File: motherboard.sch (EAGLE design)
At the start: 159 parts, among them IC1 LM2576, IC10 TUSB2046B, IC11 OPA129U, IC12 LM50, IC13 LM50, IC2 74LS595D, IC3 74LS595D, IC4 IC_FT230X-SSOP-16, IC5 VN5772AK, IC6 VN5772AK, IC7 VN5772AK, IC8 VN5772AK, IC9 VN5772AK, U2 NCP4625, U3 ATMEGA168, Y1 16Mhz, Y2 6MHz

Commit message: finished subsystem validatation
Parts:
- removed C43, C44, C45: (no value), adafruit:C-USC1206
- removed F4: 500mA, dp_devices:FUSE_PTC-1812
- removed IC11: OPA129U, burr-brown:OPA129U
- removed JP11: (no value), sparkfun:M023.5MM
- removed JP12, JP13: (no value), SparkFun-Connectors:M063.5MM-6
- removed LED1, LED2: (no value), adafruit:LEDCHIPLED_1206
- added C23: 0.1uF, adafruit:C-USC1206
- added D12, D13, D14, D15, D16, D17, D18, D19, D20, D21: (no value), adafruit:DIODESMA
- added F5, F6, F7, F8: (no value), special:FUSE2P
- added ISP2, ISP3, ISP4, ISP5: AVRISP-6, adafruit:AVRISP-6
- added R38, R39: 10k, adafruit:R-US_R1206
- added U$10, U$11, U$12, U$13, U$14, U$15, U$16, U$6, U$7, U$8, U$9: TVS, sparkfun:TVS
- added ZD1, ZD3, ZD4, ZD5: 5V, dp_devices:ZENERSOD-123
- C10, C4: value 1000uF -> 500uF
- C13: value 1000uF -> 4.7uF; device adafruit:CPOL-US153CLV-0807 -> adafruit:C-USC1206
- C14: value 0.1uF -> 500uF; device adafruit:C-USC1206 -> adafruit:CPOL-US153CLV-0807
- C15: value 1uF -> 0.1uF
- C16: value 1000uF -> 1uF; device adafruit:CPOL-US153CLV-0807 -> adafruit:C-USC1206
- C17: value 0.1uF -> 4.7uF
- C18: value 1uF -> 500uF; device adafruit:C-USC1206 -> adafruit:CPOL-US153CLV-0807
- C19: value 1000uF -> 0.1uF; device adafruit:CPOL-US153CLV-0807 -> adafruit:C-USC1206
- C20: value 0.1uF -> 1uF
- C21: value 1uF -> 4.7uF
- C24, C25, C26, C27, C28, C29, C30, C32, C33, C9: value (none) -> 47pF
- C35: value (none) -> 4.7uF
- C36: value (none) -> 0.1uF
- C39: value 4.7uF -> 500uF; device adafruit:C-USC1206 -> adafruit:CPOL-US153CLV-0807
- C40: value 4.7uF -> 0.1uF
- C41: value 4.7uF -> 1uF
- D10, D11, D2, D3, D4, D5, D6, D7, D8, D9: value BAV199 -> (none); device diode:BAV199 -> adafruit:DIODESMA
- R10, R36, R37, R6, R7, R8, R9: value 10k -> 1k
- R12, R13, R16, R17, R18, R19, R20, R21, R28, R29: value (none) -> 27
- R14, R15, R22, R23, R24, R25, R27, R30: value (none) -> 15k
- R26, R31, R5: value (none) -> 1k
- R32, R33: value (none) -> 10k
- ZD2: value (none) -> 5V
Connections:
- removed net !USB_RST: R26.2, U3.PD7(AIN1)
- removed net ARM_EN: R37.2, U3.PB1(OC1A)
- removed net CONDUCT: IC11.-IN, IC11.OUT, U3.ADC7
- removed net N$16: C18.2, D8.AC, IC8.DRAIN4@0, IC8.DRAIN4@1, IC8.DRAIN4@2, IC8.DRAIN4@3, IC8.SOURCE2@0, IC8.SOURCE2@1, JP5.2
- removed net N$17: C21.1, D11.AC, IC9.DRAIN3@0, IC9.DRAIN3@1, IC9.DRAIN3@2, IC9.DRAIN3@3, IC9.SOURCE1@0, IC9.SOURCE1@1, JP6.1
- removed net N$18: C21.2, D10.AC, IC9.DRAIN4@0, IC9.DRAIN4@1, IC9.DRAIN4@2, IC9.DRAIN4@3, IC9.SOURCE2@0, IC9.SOURCE2@1, JP6.2
- removed net N$56: JP13.5, R37.1
- removed net RANG_EN: R36.2, U3.PB0(ICP)
- new net EN1: R39.2, U3.ADC7
- new net EN2: R38.2, U3.PD7(AIN1)
- new net EN3: R33.2, U3.PB0(ICP)
- new net EN4: R32.2, U3.PB1(OC1A)
- new net N$20: C56.+, F8.1A, JP17.1, U$9.2
- new net N$54: C54.+, F6.1A, JP15.1, U$7.2
- new net N$58: ISP5.RST, R39.1, U$14.2
- net +12V: now also C13.1, C14.+, C15.1, C18.+, C19.1, C21.1, C39.+, D12.C, D14.C, D16.C, D18.C, D20.C, F5.2A, F6.2A, F7.2A, F8.2A; no longer C13.+, C14.1, C16.+, C19.+, C20.1, C39.1, C41.1, C53.+, C54.+, C55.+, C56.+, D11.C, D3.C, D5.C, D7.C, D9.C, JP14.1, JP15.1, JP16.1, JP17.1
- net +5V: now also ISP2.VCC, ISP3.VCC, ISP4.VCC, ISP5.VCC, U$16.2; no longer C43.1, C44.1, F4.2, IC11.V+, JP12.1, JP13.1
- net 0SENSE: now also IC6.SENSE, IC7.SENSE, IC8.SENSE, IC9.SENSE, R26.1, R36.1, R5.1, R6.2, R7.1, R9.1, ZD1.C
- net 1SENSE: now also R7.2, R8.1, ZD2.C; no longer IC6.SENSE, R7.1
- net 2SENSE: now also R10.1, R9.2, ZD3.C; no longer IC7.SENSE, R8.1
- net 3.3V: now also IC10.!RST
- net 3SENSE: now also R26.2, R31.1, ZD4.C; no longer IC8.SENSE, R9.1
- net 4SENSE: now also R36.2, R37.1, ZD5.C; no longer IC9.SENSE, R10.1
- net AGND: no longer C43.2, C44.2, C45.2, IC11.V-, JP11.2, R33.2, U$5.1
- net GND: now also C13.2, C14.-, C15.2, C18.-, C19.2, C21.2, C23.2, C39.-, D13.A, D15.A, D17.A, D19.A, D21.A, ISP2.GND, ISP3.GND, ISP4.GND, ISP5.GND, R31.2, R37.2, R5.2, U$10.1, U$11.1, U$12.1, U$13.1, U$14.1, U$15.1, U$16.1, U$5.1, U$6.1, U$7.1, U$8.1, U$9.1, ZD1.A, ZD3.A, ZD4.A, ZD5.A; no longer C13.-, C14.2, C16.-, C19.-, C20.2, C39.2, C41.2, D10.A, D2.A, D4.A, D6.A, D8.A, JP12.6, JP13.6, R6.2, R7.2, R9.2
- net MISO: now also ISP2.MISO, ISP3.MISO, ISP4.MISO, ISP5.MISO, U$10.2; no longer JP12.3, JP13.3
- net MOSI: now also ISP2.MOSI, ISP3.MOSI, ISP4.MOSI, ISP5.MOSI, U$11.2; no longer JP12.2, JP13.2
- net N$10: now also C20.1, D10.A, D11.C, IC8.DRAIN3@0, IC8.DRAIN3@1, IC8.DRAIN3@2, IC8.DRAIN3@3, IC8.SOURCE1@0, IC8.SOURCE1@1, JP5.1; no longer C12.2, D4.AC, IC6.DRAIN4@0, IC6.DRAIN4@1, IC6.DRAIN4@2, IC6.DRAIN4@3, IC6.SOURCE2@0, IC6.SOURCE2@1, JP3.2
- net N$11: now also D2.A, D3.C; no longer D3.AC
- net N$12: now also C20.2, D12.A, D13.C, IC8.DRAIN4@0, IC8.DRAIN4@1, IC8.DRAIN4@2, IC8.DRAIN4@3, IC8.SOURCE2@0, IC8.SOURCE2@1, JP5.2; no longer C15.1, D7.AC, IC7.DRAIN3@0, IC7.DRAIN3@1, IC7.DRAIN3@2, IC7.DRAIN3@3, IC7.SOURCE1@0, IC7.SOURCE1@1, JP4.1
- net N$13: now also D4.A, D5.C; no longer D2.AC
- net N$14: now also C41.1, D6.A, D7.C, IC9.DRAIN3@0, IC9.DRAIN3@1, IC9.DRAIN3@2, IC9.DRAIN3@3, IC9.SOURCE1@0, IC9.SOURCE1@1, JP6.1; no longer C15.2, D6.AC, IC7.DRAIN4@0, IC7.DRAIN4@1, IC7.DRAIN4@2, IC7.DRAIN4@3, IC7.SOURCE2@0, IC7.SOURCE2@1, JP4.2
- net N$15: now also C41.2, D8.A, D9.C, IC9.DRAIN4@0, IC9.DRAIN4@1, IC9.DRAIN4@2, IC9.DRAIN4@3, IC9.SOURCE2@0, IC9.SOURCE2@1, JP6.2; no longer C18.1, D9.AC, IC8.DRAIN3@0, IC8.DRAIN3@1, IC8.DRAIN3@2, IC8.DRAIN3@3, IC8.SOURCE1@0, IC8.SOURCE1@1, JP5.1
- net N$3: now also D18.A, D19.C; no longer D5.AC
- net N$38: now also C23.1; no longer R31.1, R32.1
- net N$5: now also C12.2, D20.A, D21.C, IC6.DRAIN4@0, IC6.DRAIN4@1, IC6.DRAIN4@2, IC6.DRAIN4@3, IC6.SOURCE2@0, IC6.SOURCE2@1, JP3.2; no longer IC10.!RST, R26.1, ZD2.C
- net N$50: now also C55.+, F7.1A, JP16.1, U$8.2; no longer IC4.CBUS1, LED1.C
- net N$51: now also ISP2.RST, R32.1, U$13.2; no longer IC4.CBUS2, LED2.C
- net N$52: now also ISP3.RST, R33.1, U$15.2; no longer LED1.A, R31.2
- net N$53: now also ISP4.RST, R38.1, U$12.2; no longer LED2.A, R32.2
- net N$55: now also C53.+, F5.1A, JP14.1, U$6.2; no longer JP12.5, R36.1
- net N$8: now also C16.1, D14.A, D15.C, IC7.DRAIN3@0, IC7.DRAIN3@1, IC7.DRAIN3@2, IC7.DRAIN3@3, IC7.SOURCE1@0, IC7.SOURCE1@1, JP4.1; no longer F4.1, R5.1
- net N$9: now also C16.2, D16.A, D17.C, IC7.DRAIN4@0, IC7.DRAIN4@1, IC7.DRAIN4@2, IC7.DRAIN4@3, IC7.SOURCE2@0, IC7.SOURCE2@1, JP4.2; no longer C45.1, IC11.+IN, JP11.1, R33.1, R5.2, U$5.2
- net SCK: now also ISP2.SCK, ISP3.SCK, ISP4.SCK, ISP5.SCK, U$5.2; no longer JP12.4, JP13.4
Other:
- moved on the sheet: C1, C10, C11, C12, C15, C17, C2, C20, C21, C22, C24, C25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

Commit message: updated sch
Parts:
- added SW1: FSMSM, alcoswitch:FSMSM
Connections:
- net EN1 renamed !EN1
- net EN2 renamed !EN2
- net EN3 renamed !EN3
- net EN4 renamed !EN4
- net !RST: now also SW1.S
- net GND: now also SW1.P
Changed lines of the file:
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@@
 <grid distance="0.1" unitdist="inch" unit="inch" style="lines" multiple="1" display="no" altdistance="0.01" altunitdist="inch" altunit="inch"/>
 <layers>
-<layer number="1" name="Top" color="4" fill="1" visible="yes" active="no"/>
-<layer number="2" name="Route2" color="1" fill="3" visible="yes" active="no"/>
-<layer number="3" name="Route3" color="4" fill="3" visible="yes" active="no"/>
-<layer number="4" name="Route4" color="1" fill="4" visible="yes" active="no"/>
-<layer number="5" name="Route5" color="4" fill="4" visible="yes" active="no"/>
-<layer number="6" name="Route6" color="1" fill="8" visible="yes" active="no"/>
-<layer number="7" name="Route7" color="4" fill="8" visible="yes" active="no"/>
-<layer number="8" name="Route8" color="1" fill="2" visible="yes" active="no"/>
-<layer number="9" name="Route9" color="4" fill="2" visible="yes" active="no"/>
-<layer number="10" name="Route10" color="1" fill="7" visible="yes" active="no"/>
-<layer number="11" name="Route11" color="4" fill="7" visible="yes" active="no"/>
-<layer number="12" name="Route12" color="1" fill="5" visible="yes" active="no"/>
-<layer number="13" name="Route13" color="4" fill="5" visible="yes" active="no"/>
-<layer number="14" name="Route14" color="1" fill="6" visible="yes" active="no"/>
-<layer number="15" name="Route15" color="4" fill="6" visible="yes" active="no"/>
-<layer number="16" name="Bottom" color="1" fill="1" visible="yes" active="no"/>
-<layer number="17" name="Pads" color="2" fill="1" visible="yes" active="no"/>
-<layer number="18" name="Vias" color="2" fill="1" visible="yes" active="no"/>
-<layer number="19" name="Unrouted" color="6" fill="1" visible="yes" active="no"/>
-<layer number="20" name="Dimension" color="15" fill="1" visible="yes" active="no"/>
-<layer number="21" name="tPlace" color="7" fill="1" visible="yes" active="no"/>
-<layer number="22" name="bPlace" color="7" fill="1" visible="yes" active="no"/>
-<layer number="23" name="tOrigins" color="15" fill="1" visible="yes" active="no"/>
-<layer number="24" name="bOrigins" color="15" fill="1" visible="yes" active="no"/>
-<layer number="25" name="tNames" color="7" fill="1" visible="yes" active="no"/>
-<layer number="26" name="bNames" color="7" fill="1" visible="yes" active="no"/>
-<layer number="27" name="tValues" color="7" fill="1" visible="yes" active="no"/>
-<layer number="28" name="bValues" color="7" fill="1" visible="yes" active="no"/>
+<layer number="1" name="Top" color="4" fill="1" visible="no" active="no"/>
+<layer number="2" name="Route2" color="1" fill="3" visible="no" active="no"/>
+<layer number="3" name="Route3" color="4" fill="3" visible="no" active="no"/>
+<layer number="4" name="Route4" color="1" fill="4" visible="no" active="no"/>
+<layer number="5" name="Route5" color="4" fill="4" visible="no" active="no"/>
+<layer number="6" name="Route6" color="1" fill="8" visible="no" active="no"/>
+<layer number="7" name="Route7" color="4" fill="8" visible="no" active="no"/>
+<layer number="8" name="Route8" color="1" fill="2" visible="no" active="no"/>
+<layer number="9" name="Route9" color="4" fill="2" visible="no" active="no"/>
+<layer number="10" name="Route10" color="1" fill="7" visible="no" active="no"/>
+<layer number="11" name="Route11" color="4" fill="7" visible="no" active="no"/>
+<layer number="12" name="Route12" color="1" fill="5" visible="no" active="no"/>
+<layer number="13" name="Route13" color="4" fill="5" visible="no" active="no"/>
+<layer number="14" name="Route14" color="1" fill="6" visible="no" active="no"/>
+<layer number="15" name="Route15" color="4" fill="6" visible="no" active="no"/>
+<layer number="16" name="Bottom" color="1" fill="1" visible="no" active="no"/>
+<layer number="17" name="Pads" color="2" fill="1" visible="no" active="no"/>
+<layer number="18" name="Vias" color="2" fill="1" visible="no" active="no"/>
+<layer number="19" name="Unrouted" color="6" fill="1" visible="no" active="no"/>
+<layer number="20" name="Dimension" color="15" fill="1" visible="no" active="no"/>
+<layer number="21" name="tPlace" color="7" fill="1" visible="no" active="no"/>
+<layer number="22" name="bPlace" color="7" fill="1" visible="no" active="no"/>
+<layer number="23" name="tOrigins" color="15" fill="1" visible="no" active="no"/>
+<layer number="24" name="bOrigins" color="15" fill="1" visible="no" active="no"/>
+<layer number="25" name="tNames" color="7" fill="1" visible="no" active="no"/>
+<layer number="26" name="bNames" color="7" fill="1" visible="no" active="no"/>
+<layer number="27" name="tValues" color="7" fill="1" visible="no" active="no"/>
+<layer number="28" name="bValues" color="7" fill="1" visible="no" active="no"/>
 <layer number="29" name="tStop" color="7" fill="3" visible="no" active="no"/>
 <layer number="30" name="bStop" color="7" fill="6" visible="no" active="no"/>
@@
 <layer number="35" name="tGlue" color="7" fill="4" visible="no" active="no"/>
 <layer number="36" name="bGlue" color="7" fill="5" visible="no" active="no"/>
-<layer number="37" name="tTest" color="7" fill="1" visible="yes" active="no"/>
-<layer number="38" name="bTest" color="7" fill="1" visible="yes" active="no"/>
+<layer number="37" name="tTest" color="7" fill="1" visible="no" active="no"/>
+<layer number="38" name="bTest" color="7" fill="1" visible="no" active="no"/>
 <layer number="39" name="tKeepout" color="4" fill="11" visible="no" active="no"/>
 <layer number="40" name="bKeepout" color="1" fill="11" visible="no" active="no"/>
@@
 <layer number="44" name="Drills" color="7" fill="1" visible="no" active="no"/>
 <layer number="45" name="Holes" color="7" fill="1" visible="no" active="no"/>
-<layer number="46" name="Milling" color="3" fill="1" visible="yes" active="no"/>
-<layer number="47" name="Measures" color="7" fill="1" visible="yes" active="no"/>
-<layer number="48" name="Document" color="7" fill="1" visible="yes" active="no"/>
-<layer number="49" name="Reference" color="7" fill="1" visible="yes" active="no"/>
-<layer number="50" name="dxf" color="7" fill="1" visible="yes" active="no"/>
-<layer number="51" name="tDocu" color="6" fill="1" visible="yes" active="no"/>
-<layer number="52" name="bDocu" color="7" fill="1" visible="yes" active="no"/>
-<layer number="53" name="tGND_GNDA" color="7" fill="9" visible="yes" active="no"/>
-<layer number="54" name="bGND_GNDA" color="1" fill="9" visible="yes" active="no"/>
-<layer number="56" name="wert" color="7" fill="1" visible="yes" active="no"/>
-<layer number="57" name="tCAD" color="7" fill="1" visible="yes" active="no"/>
+<layer number="46" name="Milling" color="3" fill="1" visible="no" active="no"/>
+<layer number="47" name="Measures" color="7" fill="1" visible="no" active="no"/>
+<layer number="48" name="Document" color="7" fill="1" visible="no" active="no"/>
+<layer number="49" name="Reference" color="7" fill="1" visible="no" active="no"/>
+<layer number="50" name="dxf" color="7" fill="1" visible="no" active="no"/>
+<layer number="51" name="tDocu" color="6" fill="1" visible="no" active="no"/>
+<layer number="52" name="bDocu" color="7" fill="1" visible="no" active="no"/>
+<layer number="53" name="tGND_GNDA" color="7" fill="9" visible="no" active="no"/>
+<layer number="54" name="bGND_GNDA" color="1" fill="9" visible="no" active="no"/>
+<layer number="56" name="wert" color="7" fill="1" visible="no" active="no"/>
+<layer number="57" name="tCAD" color="7" fill="1" visible="no" active="no"/>
 <layer number="91" name="Nets" color="2" fill="1" visible="yes" active="yes"/>
 <layer number="92" name="Busses" color="1" fill="1" visible="yes" active="yes"/>
@@
 <part name="D20" library="adafruit" deviceset="DIODE" device="SMA"/>
 <part name="D21" library="adafruit" deviceset="DIODE" device="SMA"/>
+<part name="SW1" library="alcoswitch" deviceset="FSMSM" device="" value=""/>
+<part name="GND117" library="sparkfun" deviceset="GND" device=""/>
 </parts>
 <sheets>
@@
 <instance part="D20" gate="G$1" x="365.76" y="127" rot="R90"/>
 <instance part="D21" gate="G$1" x="365.76" y="116.84" rot="R90"/>
+<instance part="SW1" gate="G$1" x="86.36" y="226.06"/>
+<instance part="GND117" gate="1" x="86.36" y="215.9"/>
 </instances>
 <busses>
@@
 <pinref part="GND116" gate="1" pin="GND"/>
 </segment>
+<segment>
+<pinref part="SW1" gate="G$1" pin="P"/>
+<pinref part="GND117" gate="1" pin="GND"/>
+<wire x1="86.36" y1="218.44" x2="86.36" y2="220.98" width="0.1524" layer="91"/>
+</segment>
 </net>
 <net name="+5V" class="0">
@@
 <label x="78.74" y="233.68" size="1.778" layer="95"/>
 <pinref part="U3" gate="G$1" pin="PC6(/RESET)"/>
+<pinref part="SW1" gate="G$1" pin="S"/>
+<wire x1="86.36" y1="231.14" x2="86.36" y2="233.68" width="0.1524" layer="91"/>
 </segment>
 <segment>
@@
 </segment>
 </net>
-<net name="EN4" class="0">
+<net name="!EN4" class="0">
 <segment>
 <pinref part="U3" gate="G$1" pin="PB1(OC1A)"/>
@@
 </segment>
 </net>
-<net name="EN3" class="0">
+<net name="!EN3" class="0">
 <segment>
 <pinref part="U3" gate="G$1" pin="PB0(ICP)"/>
@@
 </segment>
 </net>
-<net name="EN1" class="0">
+<net name="!EN1" class="0">
 <segment>
 <pinref part="U3" gate="G$1" pin="ADC7"/>
@@
 </segment>
 </net>
-<net name="EN2" class="0">
+<net name="!EN2" class="0">
 <segment>
 <pinref part="U3" gate="G$1" pin="PD7(AIN1)"/>

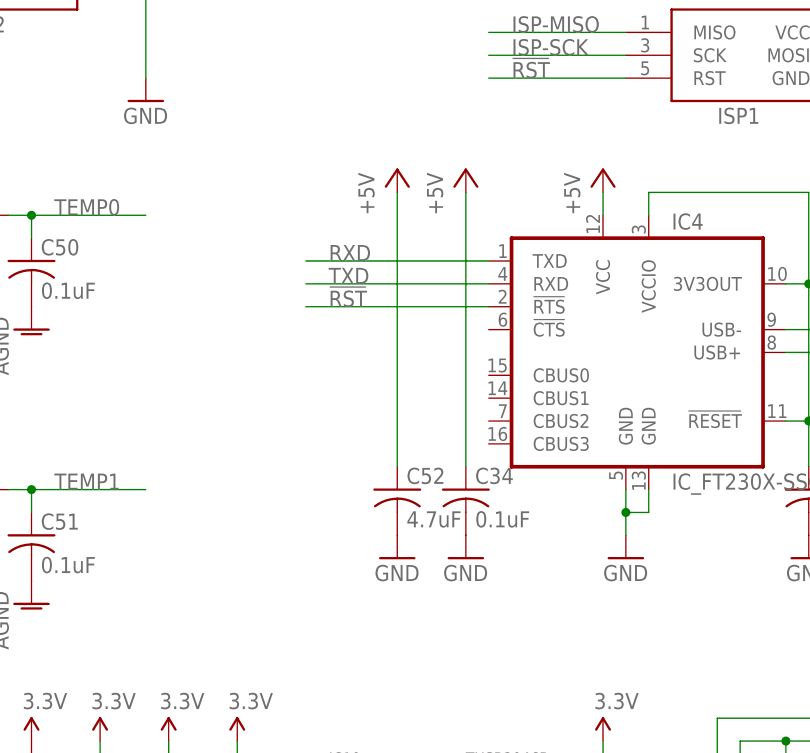
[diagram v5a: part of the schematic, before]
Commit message: added missing reset capacitor
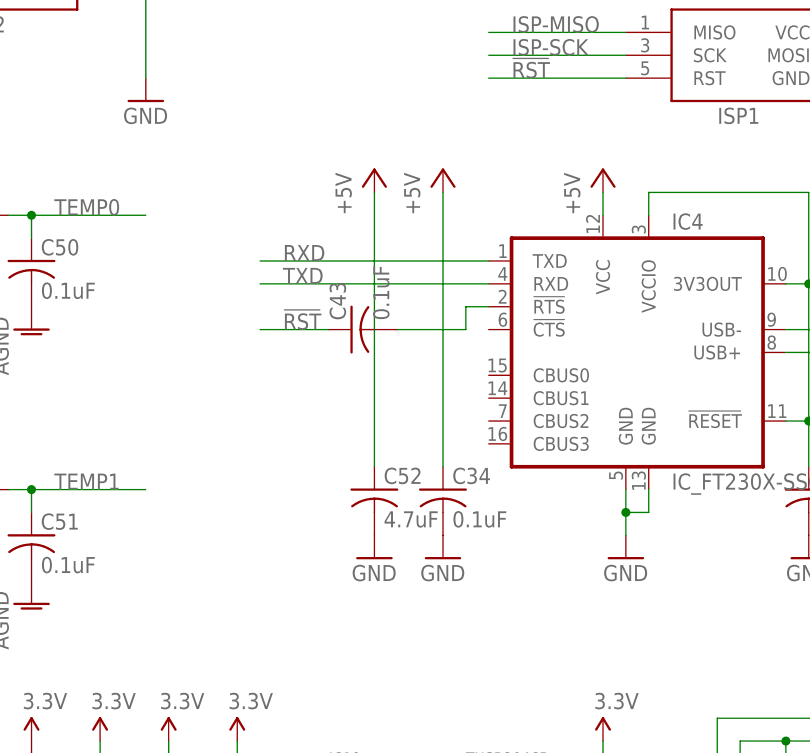
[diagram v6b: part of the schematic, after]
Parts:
- added C43: 0.1uF, adafruit:C-USC1206
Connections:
- new net N$16: C43.2, IC4.!RTS
- net !RST: now also C43.1; no longer IC4.!RTS
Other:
- moved on the sheet: C34, C52
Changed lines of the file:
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@@
 <part name="SW1" library="alcoswitch" deviceset="FSMSM" device="" value=""/>
 <part name="GND117" library="sparkfun" deviceset="GND" device=""/>
+<part name="C43" library="adafruit" deviceset="C-US" device="C1206" value="0.1uF"/>
 </parts>
 <sheets>
@@
 <instance part="GND76" gate="1" x="154.94" y="91.44"/>
 <instance part="GND77" gate="1" x="162.56" y="91.44"/>
-<instance part="C34" gate="G$1" x="88.9" y="99.06"/>
+<instance part="C34" gate="G$1" x="86.36" y="99.06"/>
 <instance part="C35" gate="G$1" x="48.26" y="45.72"/>
 <instance part="C36" gate="G$1" x="55.88" y="45.72"/>
@@
 <instance part="GND78" gate="1" x="48.26" y="2.54"/>
 <instance part="GND79" gate="1" x="55.88" y="2.54"/>
-<instance part="GND80" gate="1" x="88.9" y="91.44"/>
-<instance part="P+33" gate="1" x="88.9" y="134.62"/>
+<instance part="GND80" gate="1" x="86.36" y="91.44"/>
+<instance part="P+33" gate="1" x="86.36" y="134.62"/>
 <instance part="JP8" gate="G$1" x="205.74" y="73.66" rot="R180"/>
 <instance part="JP9" gate="G$1" x="205.74" y="50.8" rot="R180"/>
@@
 <instance part="P+40" gate="1" x="5.08" y="134.62"/>
 <instance part="P+41" gate="1" x="5.08" y="104.14"/>
-<instance part="C52" gate="G$1" x="81.28" y="99.06"/>
-<instance part="GND13" gate="1" x="81.28" y="91.44"/>
-<instance part="P+42" gate="1" x="81.28" y="134.62"/>
+<instance part="C52" gate="G$1" x="78.74" y="99.06"/>
+<instance part="GND13" gate="1" x="78.74" y="91.44"/>
+<instance part="P+42" gate="1" x="78.74" y="134.62"/>
 <instance part="JP14" gate="G$1" x="327.66" y="231.14" rot="R180"/>
 <instance part="C53" gate="G$1" x="304.8" y="226.06" rot="MR0"/>
@@
 <instance part="SW1" gate="G$1" x="86.36" y="226.06"/>
 <instance part="GND117" gate="1" x="86.36" y="215.9"/>
+<instance part="C43" gate="G$1" x="76.2" y="116.84" rot="R90"/>
 </instances>
 <busses>
@@
 <pinref part="C34" gate="G$1" pin="1"/>
 <pinref part="P+33" gate="1" pin="+5V"/>
-<wire x1="88.9" y1="132.08" x2="88.9" y2="101.6" width="0.1524" layer="91"/>
+<wire x1="86.36" y1="132.08" x2="86.36" y2="101.6" width="0.1524" layer="91"/>
 </segment>
 <segment>
@@
 <pinref part="C52" gate="G$1" pin="1"/>
 <pinref part="P+42" gate="1" pin="+5V"/>
-<wire x1="81.28" y1="132.08" x2="81.28" y2="101.6" width="0.1524" layer="91"/>
+<wire x1="78.74" y1="132.08" x2="78.74" y2="101.6" width="0.1524" layer="91"/>
 </segment>
 <segment>
@@
 </segment>
 <segment>
-<pinref part="IC4" gate="IC" pin="!RTS"/>
-<wire x1="91.44" y1="119.38" x2="71.12" y2="119.38" width="0.1524" layer="91"/>
-<label x="73.66" y="119.38" size="1.778" layer="95"/>
+<pinref part="C43" gate="G$1" pin="1"/>
+<wire x1="73.66" y1="116.84" x2="66.04" y2="116.84" width="0.1524" layer="91"/>
+<label x="68.58" y="116.84" size="1.778" layer="95"/>
 </segment>
 </net>
@@
 <segment>
 <pinref part="IC4" gate="IC" pin="TXD"/>
-<wire x1="91.44" y1="124.46" x2="71.12" y2="124.46" width="0.1524" layer="91"/>
-<label x="73.66" y="124.46" size="1.778" layer="95"/>
+<wire x1="91.44" y1="124.46" x2="66.04" y2="124.46" width="0.1524" layer="91"/>
+<label x="68.58" y="124.46" size="1.778" layer="95"/>
 </segment>
 </net>
@@
 <segment>
 <pinref part="IC4" gate="IC" pin="RXD"/>
-<wire x1="91.44" y1="121.92" x2="71.12" y2="121.92" width="0.1524" layer="91"/>
-<label x="73.66" y="121.92" size="1.778" layer="95"/>
+<wire x1="91.44" y1="121.92" x2="66.04" y2="121.92" width="0.1524" layer="91"/>
+<label x="68.58" y="121.92" size="1.778" layer="95"/>
 </segment>
 </net>
@@
 </segment>
 </net>
+<net name="N$16" class="0">
+<segment>
+<pinref part="IC4" gate="IC" pin="!RTS"/>
+<pinref part="C43" gate="G$1" pin="2"/>
+<wire x1="81.28" y1="116.84" x2="88.9" y2="116.84" width="0.1524" layer="91"/>
+<wire x1="88.9" y1="116.84" x2="88.9" y2="119.38" width="0.1524" layer="91"/>
+<wire x1="88.9" y1="119.38" x2="91.44" y2="119.38" width="0.1524" layer="91"/>
+</segment>
+</net>
